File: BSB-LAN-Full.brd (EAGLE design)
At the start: 86.5 x 33 mm, 120 parts, among them IC1 LAN8710A-EZC, IC2 TPS2375D, IC3 TX4138, IC4 SY8089AAAC, IC5 ESP32-WROOM-32E, IC6 CH340X, Q1 BC847, Q2 BC857, Q3 BC847, Q4 WPM2015-3/TR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

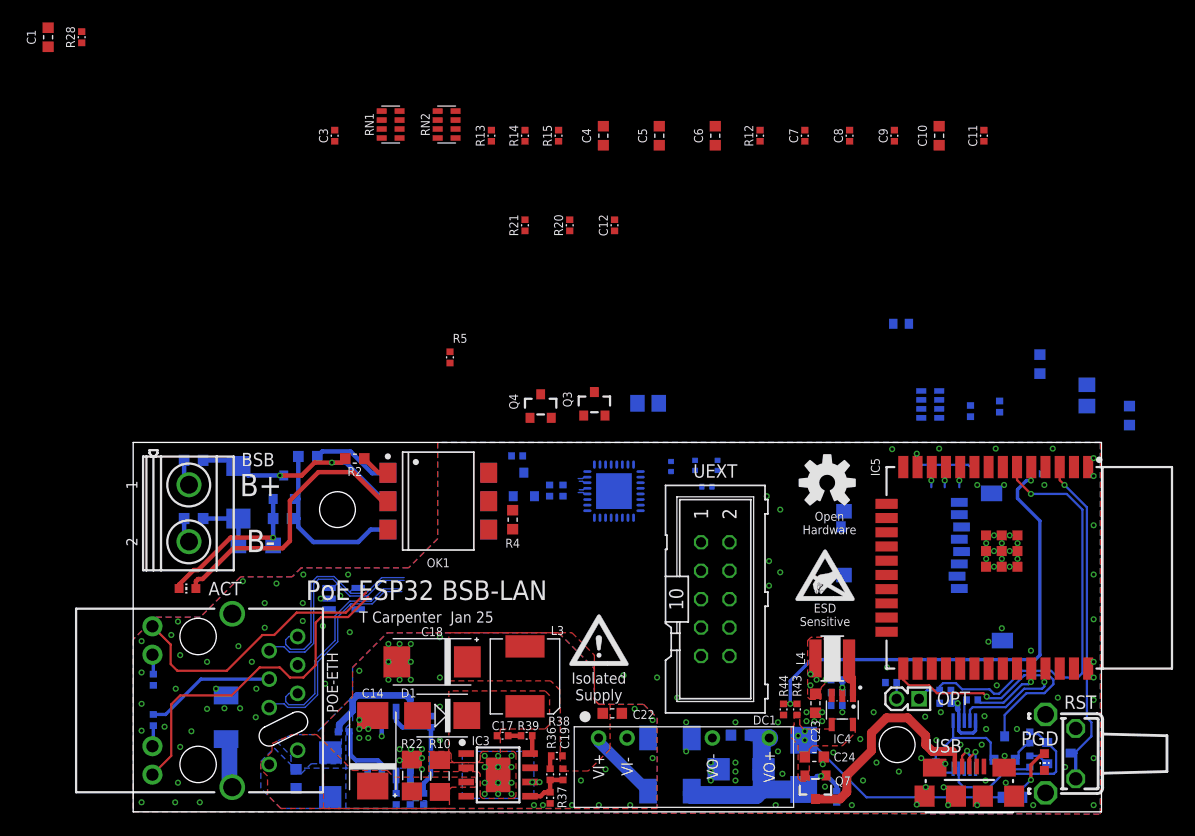
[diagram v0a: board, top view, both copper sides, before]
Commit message: Route LAN8710A connections on full PCB
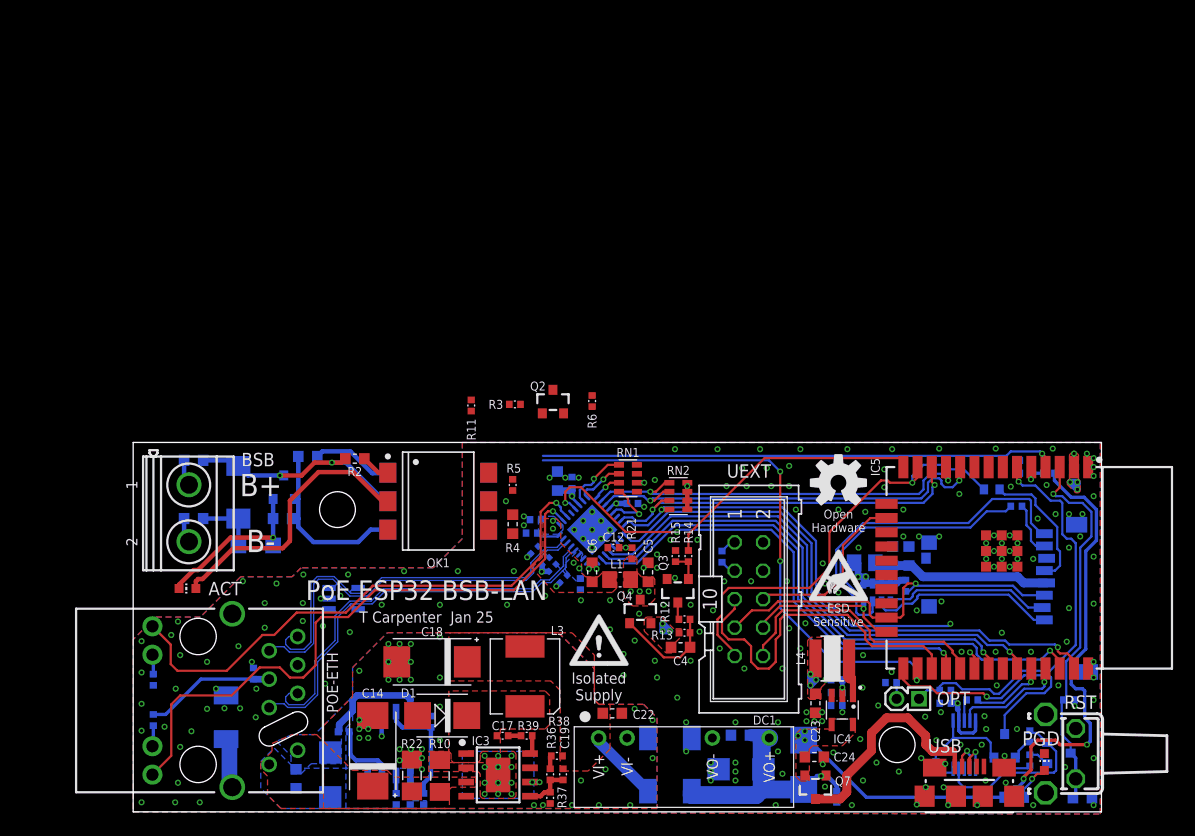
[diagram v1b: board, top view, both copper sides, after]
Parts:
- added R51: 10k, BSB-LAN:R0402
- USD: value MICROSD -> XKTF-001A
- moved C1 114.7 mm to (84.8, 1.25), flipped to the bottom, turned to 180 degrees
- moved R28 106.2 mm to (83.6, 10.0), flipped to the bottom, turned to 180 degrees
- moved C9 48.9 mm to (40.0, 20.4), flipped to the bottom, turned to 270 degrees
- moved C3 48.6 mm to (10.8, 12.3), flipped to the bottom
- moved R13 47.6 mm to (49.2, 16.0), turned to 180 degrees
- moved C4 46.2 mm to (48.9, 14.7), turned to 0 degrees
- moved C10 46.0 mm to (37.9, 29.6), flipped to the bottom
- moved C11 45.4 mm to (44.6, 27.6), flipped to the bottom, turned to 180 degrees
- moved C8 44.3 mm to (36.0, 26.1), flipped to the bottom, turned to 0 degrees
- moved R12 43.7 mm to (49.2, 17.2), turned to 0 degrees
- moved C6 40.5 mm to (41.0, 21.4)
- moved R14 40.3 mm to (49.6, 22.9), turned to 270 degrees
- moved RN2 39.1 mm to (48.7, 28.2), turned to 270 degrees
- moved C5 39.0 mm to (46.0, 21.4)
- moved R15 39.0 mm to (48.5, 22.9)
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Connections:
- new net UEXT-TX: R51.2, UEXT.3
- net +3.3V: now also R51.1; no longer UEXT.3
- net EMAC-MDIO: now also RN2.4; no longer RN2.3
- net EMAC-RX-CRSDV: now also RN2.3; no longer RN2.4
- net EMAC-RXD0: now also RN2.2; no longer RN2.1
- net EMAC-RXD1: now also RN2.1; no longer RN2.2
- net ESP-SD-DATA: now also RN3.4; no longer RN3.3
- net ETH-PHYAD1: now also RN1.1; no longer RN1.3
- net ETH-RD_N: now also R18.1; no longer R19.1
- net ETH-RD_P: now also R19.2; no longer R18.2
- net ETH-RMIISEL: now also RN1.3; no longer RN1.1
- net ETH-VDDA: now also R18.2, R19.1; no longer R18.1, R19.2
- net ETH-VDDIO: now also RN1.6; no longer RN1.8
- net GND: now also RN1.8; no longer RN1.6
- net SD-DAT1: now also RN3.3; no longer RN3.4
- net SD-DAT2: now also RN3.2; no longer RN3.1
- net SD-DAT3: now also RN3.1; no longer RN3.2
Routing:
- net EMAC-TXD1: track 0.00 -> 51.9 mm, vias 0 -> 1
- net EMAC-MDC: track 0.00 -> 50.5 mm, vias 0 -> 1
- net BSB-TXD: track 0.00 -> 50.4 mm, vias 0 -> 3
- net EMAC-TXEN: track 0.00 -> 46.7 mm, vias 0 -> 1
- net EMAC-CLKOUT: track 0.00 -> 46.4 mm, vias 0 -> 3
- net BSB-RXD: track 0.00 -> 46.2 mm, vias 0 -> 1
- net EMAC-TXD0: track 0.00 -> 44.7 mm, vias 0 -> 1
- net EMAC-MDIO: track 0.00 -> 42.7 mm, vias 0 -> 3
- net PWR-SNS: track 45.5 -> 3.91 mm, vias 2 -> 1
- net +5.0V: track 19.9 -> 59.7 mm, vias 3 -> 5
- net ESP-SD-DATA: track 0.00 -> 36.3 mm, vias 0 -> 1
- net EMAC-RXD0: track 1.83 -> 37.5 mm, vias 1 -> 2
- net ESP-SD-CMD: track 0.00 -> 34.6 mm, vias 0 -> 1
- net EMAC-RXD1: track 1.85 -> 36.2 mm, vias 1 -> 2
- net ESP-SD-CLK: track 7.28 -> 39.4 mm
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- added copper zone on layer 1, net ETH-VDDA
- added copper zone on layer 16, net ETH-VDDA
- added copper zone on layer 1, net ETH-VDDIO
- added copper zone on layer 2, net ETH-VDDIO

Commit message: Finish Routing Full Board
Route the remaining BSB components, and also fix arrangement of parts on rear of the board which were encroaching the DIN frame keep-out.
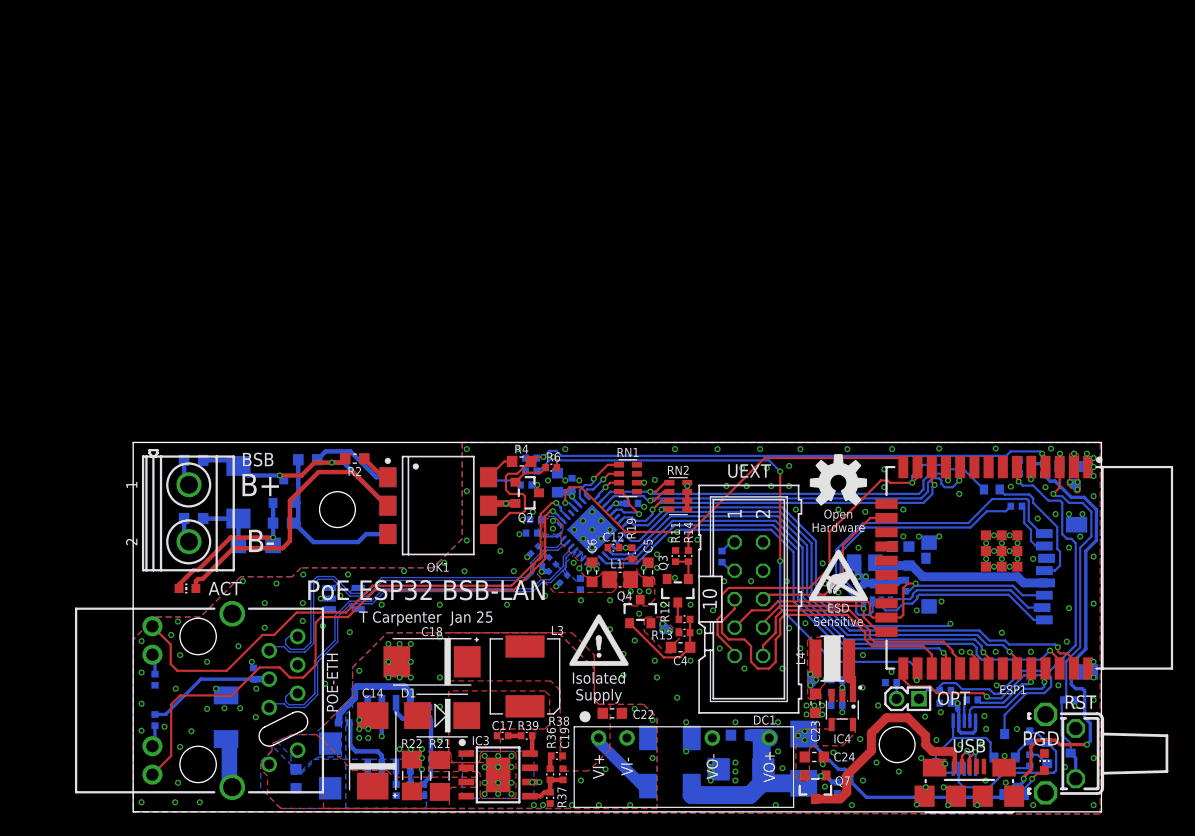
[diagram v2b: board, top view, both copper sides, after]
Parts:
- C10: value 2.2uF -> 0.1uF; device BSB-LAN:C0603 -> BSB-LAN:C0402
- C7: value 0.1uF -> 2.2uF; device BSB-LAN:C0402 -> BSB-LAN:C0603
- R10: value 0.03R 1% -> 10R; device BSB-LAN:R1206 -> BSB-LAN:R0603
- R11: value 4.7k -> 10k
- R15: value 10k -> 49.9R; device BSB-LAN:R0402 -> BSB-LAN:R0402L
- R19: value 49.9R -> 10k; device BSB-LAN:R0402L -> BSB-LAN:R0402
- R21: value 10k -> 0.03R 1%; device BSB-LAN:R0402 -> BSB-LAN:R1206
- R8: value 10R -> 4.7k; device BSB-LAN:R0603 -> BSB-LAN:R0402
- moved R10 35.8 mm to (5.40, 31.4), flipped to the bottom, turned to 180 degrees
- moved R8 30.2 mm to (35.5, 30.4)
- moved C1 29.6 mm to (83.6, 30.9)
- moved R21 26.3 mm to (27.4, 3.20), turned to 90 degrees
- moved R11 22.7 mm to (48.5, 22.9)
- moved R15 10.2 mm to (38.5, 20.8), flipped to the bottom, turned to 315 degrees
- moved R19 8.71 mm to (44.5, 23.1), flipped to the top, turned to 270 degrees
- moved Q2 8.43 mm to (35.1, 28.5), turned to 270 degrees
- moved R3 7.27 mm to (35.1, 29.2), flipped to the bottom
- moved R6 6.98 mm to (37.4, 30.8), turned to 0 degrees
- moved R4 5.66 mm to (34.7, 31.3), turned to 180 degrees
- moved R5 2.91 mm to (35.5, 31.6), flipped to the bottom, turned to 0 degrees
- moved R16 1.41 mm to (37.5, 21.8), turned to 135 degrees
- moved R18 1.41 mm to (35.9, 23.4), turned to 135 degrees
- moved C10 1.32 mm to (39.2, 29.3)
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- renumbered IC5 to ESP1
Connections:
- net BSB+: now also R10.2; no longer R8.2
- net BSB-TXD: now also R8.2; no longer R11.2
- net CON-BSB+: now also R10.1; no longer R8.1
- net ETH-PWR-B: now also R11.1; no longer R15.1
- net ETH-RD_N: now also R17.1; no longer R18.1
- net ETH-RD_P: now also R18.2; no longer R19.2
- net ETH-RST: now also R19.1; no longer R21.1
- net ETH-TD_N: now also R15.1; no longer R16.1
- net ETH-TD_P: now also R16.2; no longer R17.2
- net ETH-VDDA: now also R15.2, R16.1, R17.2, R18.1; no longer R16.2, R17.1, R18.2, R19.1
- net ETH-VDDIO: now also R19.2; no longer R21.2
- net GND: now also R11.2, R8.1; no longer R11.1, R15.2
- net POE-DC-ILIM: now also R21.2; no longer R10.2
- net POE-V+: now also R21.1; no longer R10.1
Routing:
- net +3.3V: track 23.1 -> 53.3 mm
- net BSB-RXD: track 46.2 -> 59.9 mm, vias 1 -> 2
- net TXD-A: track 0.00 -> 3.31 mm
- net TXD-B: track 0.00 -> 3.24 mm
- net RXD-B: track 0.00 -> 2.68 mm
- net BSB-TXD: track 50.4 -> 52.7 mm, vias 3 -> 4
- net +5.0V: track 59.7 -> 61.1 mm
- net TXD-C: track 0.00 -> 1.26 mm, vias 0 -> 1
- net PWR-SNS: track 3.91 -> 4.81 mm
- net POE-PG: track 23.0 -> 23.8 mm
- net +5.0V-POE: track 22.5 -> 21.8 mm
- net ESP-EN: track 34.0 -> 34.6 mm, vias 1 -> 2

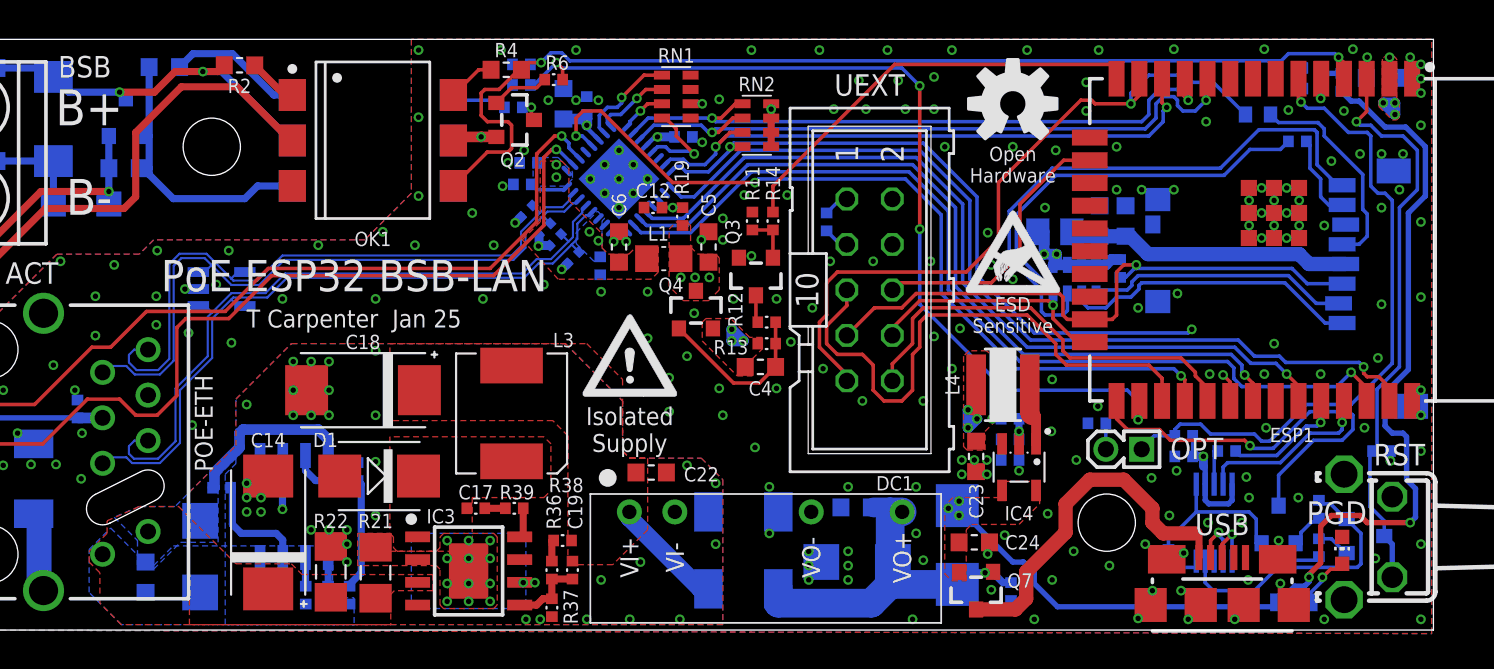
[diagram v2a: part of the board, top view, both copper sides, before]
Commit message: Improve EMAC Clock Routing
Ensure contiguous ground plane underneath as it transitions across the top layer.
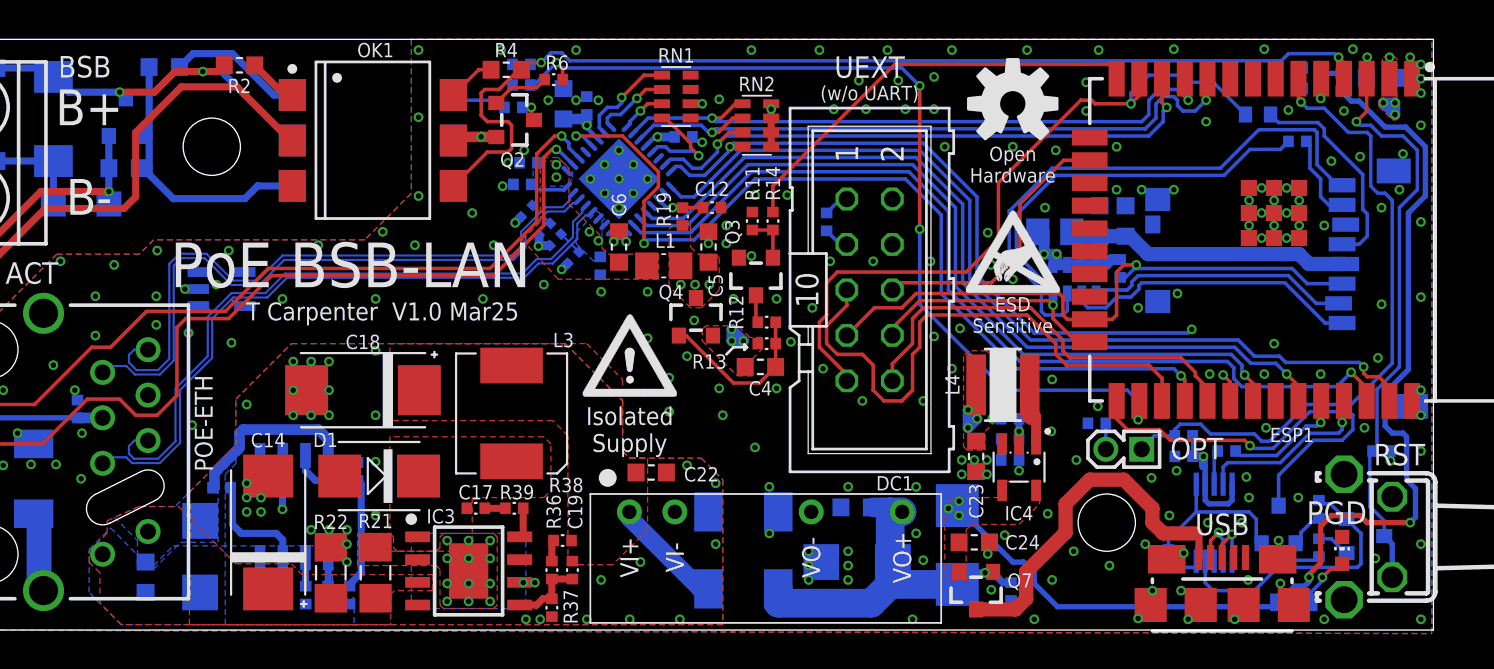
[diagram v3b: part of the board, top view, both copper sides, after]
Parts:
- moved C12 3.30 mm to (46.2, 23.6), turned to 0 degrees
- moved Q4 0.40 mm to (45.3, 17.4)
- moved L1 0.40 mm to (43.5, 20.4)
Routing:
- net EMAC-CLKOUT: track 46.4 -> 51.0 mm
- net GND: track 0.00 -> 4.00 mm, vias 224 -> 223
- net ETH-RST: track 2.13 -> 3.23 mm
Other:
- board text added: "(w/o UART)"
- board text added: "PoE BSB-LAN"
- board text added: "T Carpenter V1.0 Mar25"
- board text removed: "PoE ESP32 BSB-LAN"
- board text removed: "T Carpenter Jan 25"
